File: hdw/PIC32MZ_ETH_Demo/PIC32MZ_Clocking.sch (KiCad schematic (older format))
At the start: 15 parts

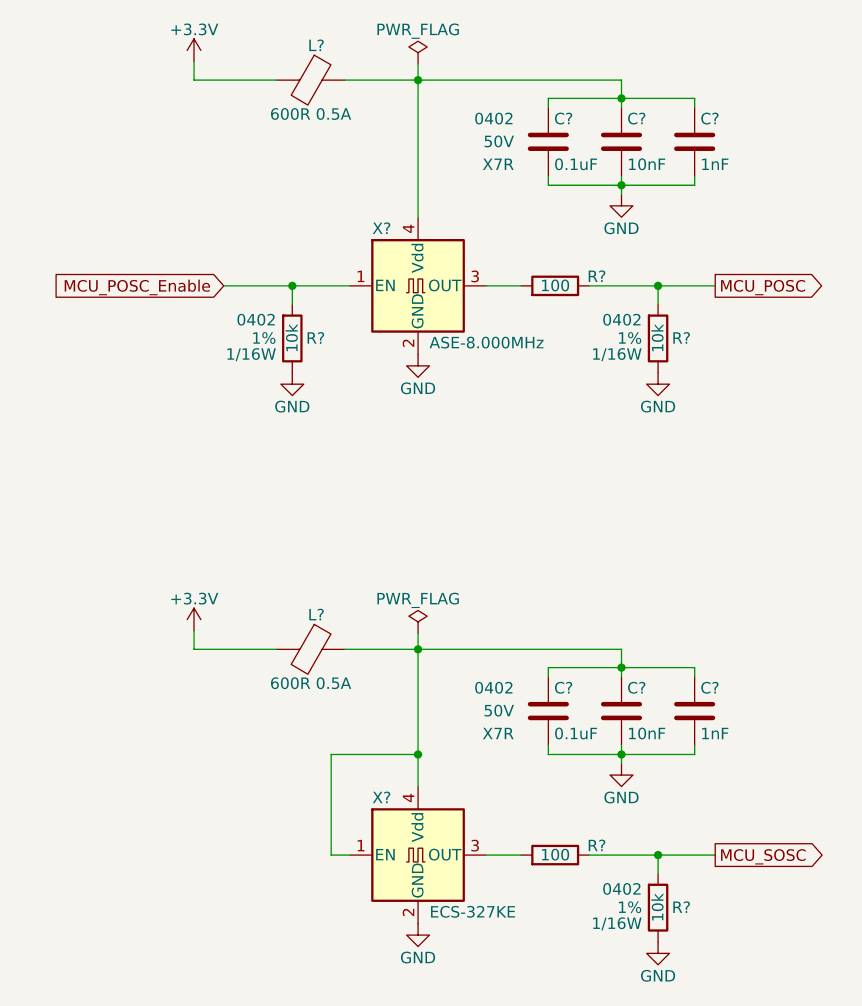
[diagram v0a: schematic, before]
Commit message: More schematic tweaks, followed PHY design guide
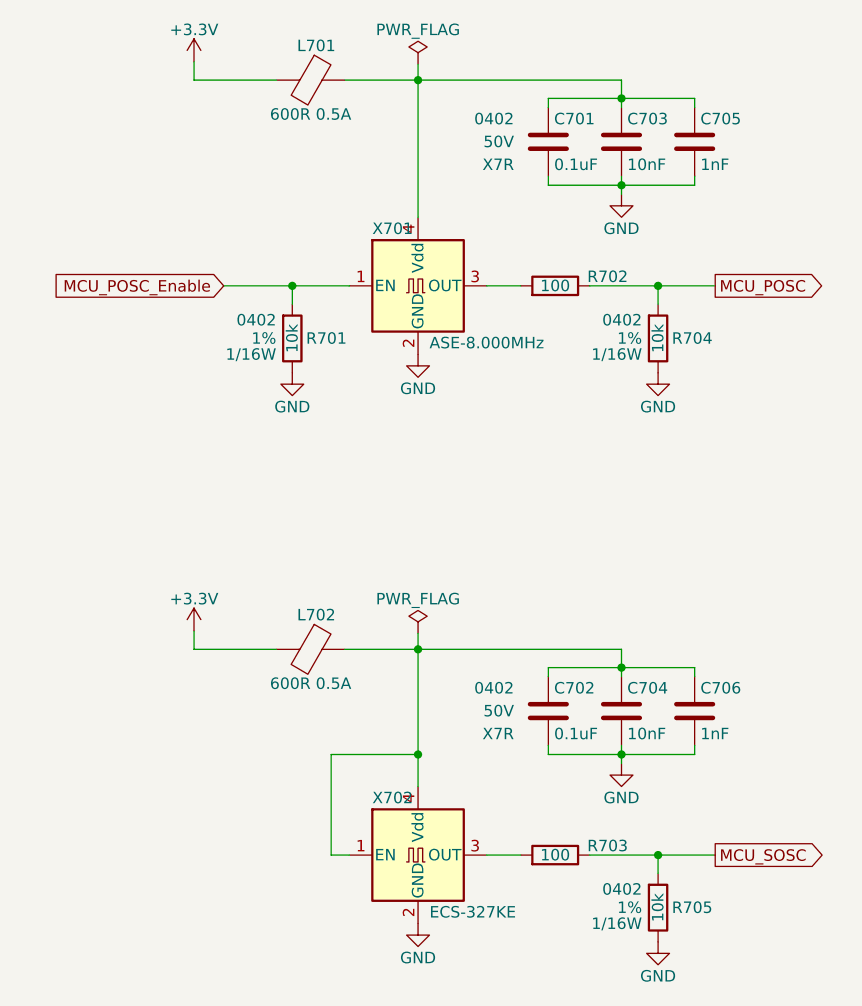
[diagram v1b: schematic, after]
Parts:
- gave numbers to parts that had none: 15
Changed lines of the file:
@@
 EESchema Schematic File Version 4
+LIBS:PIC32MZ_ETH_Demo-cache
 EELAYER 30 0
 EELAYER END
@@
 $EndDescr
 $Comp
-L Oscillator:ASE-xxxMHz X?
+L Oscillator:ASE-xxxMHz X701
 U 1 1 5E015C3C
 P 5510 2700
-F 0 "X?" H 5310 2950 50  0000 L CNN
+F 0 "X701" H 5310 2950 50  0000 L CNN
 F 1 "ASE-8.000MHz" H 5560 2450 50  0000 L CNN
 F 2 "Oscillator:Oscillator_SMD_Abracon_ASE-4Pin_3.2x2.5mm" H 6210 2350 50  0001 C CNN
@@
 $EndComp
 $Comp
-L power:GND #PWR?
+L power:GND #PWR0704
 U 1 1 5E01A3D9
 P 5510 3000
-F 0 "#PWR?" H 5510 2750 50  0001 C CNN
+F 0 "#PWR0704" H 5510 2750 50  0001 C CNN
 F 1 "GND" H 5510 2850 50  0000 C CNN
 F 2 "" H 5510 3000 50  0001 C CNN
@@
 AR Path="/5CB7A8BC/5E021EF5" Ref="R?"  Part="1"
 AR Path="/5E01BCC3/5E021EF5" Ref="R?"  Part="1"
-AR Path="/5E697952/5E021EF5" Ref="R?"  Part="1"
-F 0 "R?" H 6500 2930 50  0000 R CNN
+AR Path="/5E697952/5E021EF5" Ref="R704"  Part="1"
+F 0 "R704" H 6500 2930 50  0000 R CNN
 F 1 "10k" V 6560 2930 50  0000 C CNN
 F 2 "Resistors_SMD:R_0402" H 6560 2930 50  0001 C CNN
@@
 AR Path="/5CB7A8BC/5E021EFB" Ref="#PWR?"  Part="1"
 AR Path="/5E01BCC3/5E021EFB" Ref="#PWR?"  Part="1"
-AR Path="/5E697952/5E021EFB" Ref="#PWR?"  Part="1"
-F 0 "#PWR?" H 6560 2830 50  0001 C CNN
+AR Path="/5E697952/5E021EFB" Ref="#PWR0708"  Part="1"
+F 0 "#PWR0708" H 6560 2830 50  0001 C CNN
 F 1 "GND" H 6560 2930 50  0000 C CNN
 F 2 "" H 6560 3080 50  0001 C CNN
@@
 AR Path="/5CAD2DA3/5E024C29" Ref="R?"  Part="1"
 AR Path="/5E01BCC3/5E024C29" Ref="R?"  Part="1"
-AR Path="/5E697952/5E024C29" Ref="R?"  Part="1"
-F 0 "R?" V 6070 2560 50  0000 R CNN
+AR Path="/5E697952/5E024C29" Ref="R702"  Part="1"
+F 0 "R702" V 6070 2560 50  0000 R CNN
 F 1 "100" V 6110 2700 50  0000 C CNN
 F 2 "Resistors_SMD:R_0402" H 6110 2700 50  0001 C CNN
@@
 AR Path="/5CB7A8BC/5E0269C4" Ref="R?"  Part="1"
 AR Path="/5E01BCC3/5E0269C4" Ref="R?"  Part="1"
-AR Path="/5E697952/5E0269C4" Ref="R?"  Part="1"
-F 0 "R?" H 4900 2930 50  0000 R CNN
+AR Path="/5E697952/5E0269C4" Ref="R701"  Part="1"
+F 0 "R701" H 4900 2930 50  0000 R CNN
 F 1 "10k" V 4960 2930 50  0000 C CNN
 F 2 "Resistors_SMD:R_0402" H 4960 2930 50  0001 C CNN
@@
 AR Path="/5CB7A8BC/5E0269CA" Ref="#PWR?"  Part="1"
 AR Path="/5E01BCC3/5E0269CA" Ref="#PWR?"  Part="1"
-AR Path="/5E697952/5E0269CA" Ref="#PWR?"  Part="1"
-F 0 "#PWR?" H 4960 2830 50  0001 C CNN
+AR Path="/5E697952/5E0269CA" Ref="#PWR0703"  Part="1"
+F 0 "#PWR0703" H 4960 2830 50  0001 C CNN
 F 1 "GND" H 4960 2930 50  0000 C CNN
 F 2 "" H 4960 3080 50  0001 C CNN
@@
 AR Path="/5CB25152/5E03ADCE" Ref="#PWR?"  Part="1"
 AR Path="/5E01BCC3/5E03ADCE" Ref="#PWR?"  Part="1"
-AR Path="/5E697952/5E03ADCE" Ref="#PWR?"  Part="1"
-F 0 "#PWR?" H 6400 2050 50  0001 C CNN
+AR Path="/5E697952/5E03ADCE" Ref="#PWR0706"  Part="1"
+F 0 "#PWR0706" H 6400 2050 50  0001 C CNN
 F 1 "GND" H 6400 2150 50  0000 C CNN
 F 2 "" H 6400 2300 50  0000 C CNN
@@
 AR Path="/5CB25152/5E03ADD8" Ref="C?"  Part="1"
 AR Path="/5E01BCC3/5E03ADD8" Ref="C?"  Part="1"
-AR Path="/5E697952/5E03ADD8" Ref="C?"  Part="1"
-F 0 "C?" H 6105 2170 50  0000 L CNN
+AR Path="/5E697952/5E03ADD8" Ref="C701"  Part="1"
+F 0 "C701" H 6105 2170 50  0000 L CNN
 F 1 "0.1uF" H 6105 1970 50  0000 L CNN
 F 2 "Capacitors_SMD:C_0402" H 6118 1920 50  0001 C CNN
@@
 AR Path="/5CB25152/5E03ADE2" Ref="C?"  Part="1"
 AR Path="/5E01BCC3/5E03ADE2" Ref="C?"  Part="1"
-AR Path="/5E697952/5E03ADE2" Ref="C?"  Part="1"
-F 0 "C?" H 6745 2170 50  0000 L CNN
+AR Path="/5E697952/5E03ADE2" Ref="C705"  Part="1"
+F 0 "C705" H 6745 2170 50  0000 L CNN
 F 1 "1nF" H 6745 1970 50  0000 L CNN
 F 2 "Capacitors_SMD:C_0402" H 6758 1920 50  0001 C CNN
@@
 AR Path="/5CB25152/5E03ADEC" Ref="C?"  Part="1"
 AR Path="/5E01BCC3/5E03ADEC" Ref="C?"  Part="1"
-AR Path="/5E697952/5E03ADEC" Ref="C?"  Part="1"
-F 0 "C?" H 6425 2170 50  0000 L CNN
+AR Path="/5E697952/5E03ADEC" Ref="C703"  Part="1"
+F 0 "C703" H 6425 2170 50  0000 L CNN
 F 1 "10nF" H 6425 1970 50  0000 L CNN
 F 2 "Capacitors_SMD:C_0402" H 6438 1920 50  0001 C CNN
@@
 AR Path="/5CAD2D97/5E053473" Ref="L?"  Part="1"
 AR Path="/5E01BCC3/5E053473" Ref="L?"  Part="1"
-AR Path="/5E697952/5E053473" Ref="L?"  Part="1"
-F 0 "L?" V 4890 1825 50  0000 C CNN
+AR Path="/5E697952/5E053473" Ref="L701"  Part="1"
+F 0 "L701" V 4890 1825 50  0000 C CNN
 F 1 "600R 0.5A" V 5190 1800 50  0000 C CNN
 F 2 "Inductors_SMD:L_0603" V 4970 1800 50  0001 C CNN
@@
 	4530 1800 4890 1800
 $Comp
-L power:GND #PWR?
+L power:GND #PWR0705
 U 1 1 5E056297
 P 5510 5490
-F 0 "#PWR?" H 5510 5240 50  0001 C CNN
+F 0 "#PWR0705" H 5510 5240 50  0001 C CNN
 F 1 "GND" H 5510 5340 50  0000 C CNN
 F 2 "" H 5510 5490 50  0001 C CNN
@@
 AR Path="/5CB7A8BC/5E0562A6" Ref="R?"  Part="1"
 AR Path="/5E01BCC3/5E0562A6" Ref="R?"  Part="1"
-AR Path="/5E697952/5E0562A6" Ref="R?"  Part="1"
-F 0 "R?" H 6500 5420 50  0000 R CNN
+AR Path="/5E697952/5E0562A6" Ref="R705"  Part="1"
+F 0 "R705" H 6500 5420 50  0000 R CNN
 F 1 "10k" V 6560 5420 50  0000 C CNN
 F 2 "Resistors_SMD:R_0402" H 6560 5420 50  0001 C CNN
@@
 AR Path="/5CB7A8BC/5E0562B0" Ref="#PWR?"  Part="1"
 AR Path="/5E01BCC3/5E0562B0" Ref="#PWR?"  Part="1"
-AR Path="/5E697952/5E0562B0" Ref="#PWR?"  Part="1"
-F 0 "#PWR?" H 6560 5320 50  0001 C CNN
+AR Path="/5E697952/5E0562B0" Ref="#PWR0709"  Part="1"
+F 0 "#PWR0709" H 6560 5320 50  0001 C CNN
 F 1 "GND" H 6560 5420 50  0000 C CNN
 F 2 "" H 6560 5570 50  0001 C CNN
@@
 AR Path="/5CAD2DA3/5E0562C1" Ref="R?"  Part="1"
 AR Path="/5E01BCC3/5E0562C1" Ref="R?"  Part="1"
-AR Path="/5E697952/5E0562C1" Ref="R?"  Part="1"
-F 0 "R?" V 6070 5050 50  0000 R CNN
+AR Path="/5E697952/5E0562C1" Ref="R703"  Part="1"
+F 0 "R703" V 6070 5050 50  0000 R CNN
 F 1 "100" V 6110 5190 50  0000 C CNN
 F 2 "Resistors_SMD:R_0402" H 6110 5190 50  0001 C CNN
@@
 AR Path="/5CB25152/5E0562EA" Ref="#PWR?"  Part="1"
 AR Path="/5E01BCC3/5E0562EA" Ref="#PWR?"  Part="1"
-AR Path="/5E697952/5E0562EA" Ref="#PWR?"  Part="1"
-F 0 "#PWR?" H 6400 4540 50  0001 C CNN
+AR Path="/5E697952/5E0562EA" Ref="#PWR0707"  Part="1"
+F 0 "#PWR0707" H 6400 4540 50  0001 C CNN
 F 1 "GND" H 6400 4640 50  0000 C CNN
 F 2 "" H 6400 4790 50  0000 C CNN
@@
 AR Path="/5CB25152/5E0562F8" Ref="C?"  Part="1"
 AR Path="/5E01BCC3/5E0562F8" Ref="C?"  Part="1"
-AR Path="/5E697952/5E0562F8" Ref="C?"  Part="1"
-F 0 "C?" H 6105 4660 50  0000 L CNN
+AR Path="/5E697952/5E0562F8" Ref="C702"  Part="1"
+F 0 "C702" H 6105 4660 50  0000 L CNN
 F 1 "0.1uF" H 6105 4460 50  0000 L CNN
 F 2 "Capacitors_SMD:C_0402" H 6118 4410 50  0001 C CNN
@@
 AR Path="/5CB25152/5E056306" Ref="C?"  Part="1"
 AR Path="/5E01BCC3/5E056306" Ref="C?"  Part="1"
-AR Path="/5E697952/5E056306" Ref="C?"  Part="1"
-F 0 "C?" H 6745 4660 50  0000 L CNN
+AR Path="/5E697952/5E056306" Ref="C706"  Part="1"
+F 0 "C706" H 6745 4660 50  0000 L CNN
 F 1 "1nF" H 6745 4460 50  0000 L CNN
 F 2 "Capacitors_SMD:C_0402" H 6758 4410 50  0001 C CNN
@@
 AR Path="/5CB25152/5E056314" Ref="C?"  Part="1"
 AR Path="/5E01BCC3/5E056314" Ref="C?"  Part="1"
-AR Path="/5E697952/5E056314" Ref="C?"  Part="1"
-F 0 "C?" H 6425 4660 50  0000 L CNN
+AR Path="/5E697952/5E056314" Ref="C704"  Part="1"
+F 0 "C704" H 6425 4660 50  0000 L CNN
 F 1 "10nF" H 6425 4460 50  0000 L CNN
 F 2 "Capacitors_SMD:C_0402" H 6438 4410 50  0001 C CNN
@@
 AR Path="/5CAD2D97/5E05632C" Ref="L?"  Part="1"
 AR Path="/5E01BCC3/5E05632C" Ref="L?"  Part="1"
-AR Path="/5E697952/5E05632C" Ref="L?"  Part="1"
-F 0 "L?" V 4890 4315 50  0000 C CNN
+AR Path="/5E697952/5E05632C" Ref="L702"  Part="1"
+F 0 "L702" V 4890 4315 50  0000 C CNN
 F 1 "600R 0.5A" V 5190 4290 50  0000 C CNN
 F 2 "Inductors_SMD:L_0603" V 4970 4290 50  0001 C CNN
@@
 	4530 4290 4890 4290
 $Comp
-L Custom_Library:ECS-327KE X?
+L Custom_Library:ECS-327KE X702
 U 1 1 5E05D8E0
 P 5510 5190
-F 0 "X?" H 5310 5440 50  0000 L CNN
+F 0 "X702" H 5310 5440 50  0000 L CNN
 F 1 "ECS-327KE" H 5560 4940 50  0000 L CNN
 F 2 "Custom Footprints Library:ECS-327KE" H 6210 4840 50  0001 C CNN
@@
 	5510 4750 5510 4890
 $Comp
-L power:PWR_FLAG #FLG?
+L power:PWR_FLAG #FLG0702
 U 1 1 5E43B375
 P 5510 4220
-F 0 "#FLG?" H 5510 4295 50  0001 C CNN
+F 0 "#FLG0702" H 5510 4295 50  0001 C CNN
 F 1 "PWR_FLAG" H 5510 4370 50  0000 C CNN
 F 2 "" H 5510 4220 50  0001 C CNN
@@
 	5510 4220 5510 4290
 $Comp
-L power:PWR_FLAG #FLG?
+L power:PWR_FLAG #FLG0701
 U 1 1 5E43F288
 P 5510 1730
-F 0 "#FLG?" H 5510 1805 50  0001 C CNN
+F 0 "#FLG0701" H 5510 1805 50  0001 C CNN
 F 1 "PWR_FLAG" H 5510 1880 50  0000 C CNN
 F 2 "" H 5510 1730 50  0001 C CNN
@@
 	5510 1730 5510 1800
 $Comp
-L power:+3.3V #PWR?
+L power:+3.3V #PWR0701
 U 1 1 5E6E8CA9
 P 4530 1720
-F 0 "#PWR?" H 4530 1570 50  0001 C CNN
+F 0 "#PWR0701" H 4530 1570 50  0001 C CNN
 F 1 "+3.3V" H 4530 1860 50  0000 C CNN
 F 2 "" H 4530 1720 50  0001 C CNN
@@
 $EndComp
 $Comp
-L power:+3.3V #PWR?
+L power:+3.3V #PWR0702
 U 1 1 5E6E96AD
 P 4530 4210
-F 0 "#PWR?" H 4530 4060 50  0001 C CNN
+F 0 "#PWR0702" H 4530 4060 50  0001 C CNN
 F 1 "+3.3V" H 4530 4350 50  0000 C CNN
 F 2 "" H 4530 4210 50  0001 C CNN

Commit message: Populated digi-key pn's
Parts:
- C701, C702: Digi-Key PN (none) -> 490-10701-1-ND
- C703, C704: Digi-Key PN (none) -> 490-13295-1-ND
- C705, C706: Digi-Key PN (none) -> 399-1032-1-ND
- L701, L702: footprint Inductors_SMD:L_0603 -> Inductors_SMD:L_0402; Digi-Key PN (none) -> 490-5441-1-ND
- R701, R704, R705: Digi-Key PN (none) -> RMCF0402FT10K0CT-ND
- R702, R703: Digi-Key PN (none) -> 541-100LCT-ND
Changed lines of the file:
@@
 F 5 "1%" H 6630 2930 50  0000 L CNN "Tolerance"
 F 6 "1/16W" H 6630 2860 50  0000 L CNN "Wattage"
-F 7 "" H 6560 2930 50  0001 C CNN "Digi-Key PN"
+F 7 "RMCF0402FT10K0CT-ND" H 6560 2930 50  0001 C CNN "Digi-Key PN"
 	1    6560 2930
 	-1   0    0    -1
@@
 F 5 "1%" V 6310 2700 50  0001 C CNN "Tolerance"
 F 6 "1/16W" V 6410 2700 50  0001 C CNN "Wattage"
-F 7 "" H 6410 3100 60  0001 C CNN "Digi-Key PN"
+F 7 "541-100LCT-ND" H 6410 3100 60  0001 C CNN "Digi-Key PN"
 	1    6110 2700
 	0    -1   1    0
@@
 F 5 "1%" H 5030 2930 50  0000 L CNN "Tolerance"
 F 6 "1/16W" H 5030 2860 50  0000 L CNN "Wattage"
-F 7 "" H 4960 2930 50  0001 C CNN "Digi-Key PN"
+F 7 "RMCF0402FT10K0CT-ND" H 4960 2930 50  0001 C CNN "Digi-Key PN"
 	1    4960 2930
 	-1   0    0    -1
@@
 F 5 "50V" H 5930 2070 50  0000 R CNN "Voltage"
 F 6 "X7R" H 5930 1970 50  0000 R CNN "Dielectric"
-F 7 "" H 2170 -4810 50  0001 C CNN "Digi-Key PN"
+F 7 "490-10701-1-ND" H 2170 -4810 50  0001 C CNN "Digi-Key PN"
 	1    6080 2070
 	1    0    0    -1
@@
 F 5 "50V" H 6570 2070 50  0001 R CNN "Voltage"
 F 6 "X7R" H 6570 1970 50  0001 R CNN "Dielectric"
-F 7 "" H 2170 -4810 50  0001 C CNN "Digi-Key PN"
+F 7 "399-1032-1-ND" H 2170 -4810 50  0001 C CNN "Digi-Key PN"
 	1    6720 2070
 	1    0    0    -1
@@
 F 5 "50V" H 6250 2070 50  0001 R CNN "Voltage"
 F 6 "X7R" H 6250 1970 50  0001 R CNN "Dielectric"
-F 7 "" H 2170 -4810 50  0001 C CNN "Digi-Key PN"
+F 7 "490-13295-1-ND" H 2170 -4810 50  0001 C CNN "Digi-Key PN"
 	1    6400 2070
 	1    0    0    -1
@@
 F 0 "L701" V 4890 1825 50  0000 C CNN
 F 1 "600R 0.5A" V 5190 1800 50  0000 C CNN
-F 2 "Inductors_SMD:L_0603" V 4970 1800 50  0001 C CNN
+F 2 "Inductors_SMD:L_0402" V 4970 1800 50  0001 C CNN
 F 3 "~" H 5040 1800 50  0001 C CNN
-F 4 "" H -3150 -1290 50  0001 C CNN "Digi-Key PN"
+F 4 "490-5441-1-ND" H -3150 -1290 50  0001 C CNN "Digi-Key PN"
 	1    5040 1800
 	0    1    1    0
@@
 F 5 "1%" H 6630 5420 50  0000 L CNN "Tolerance"
 F 6 "1/16W" H 6630 5350 50  0000 L CNN "Wattage"
-F 7 "" H 6560 5420 50  0001 C CNN "Digi-Key PN"
+F 7 "RMCF0402FT10K0CT-ND" H 6560 5420 50  0001 C CNN "Digi-Key PN"
 	1    6560 5420
 	-1   0    0    -1
@@
 F 5 "1%" V 6310 5190 50  0001 C CNN "Tolerance"
 F 6 "1/16W" V 6410 5190 50  0001 C CNN "Wattage"
-F 7 "" H 6410 5590 60  0001 C CNN "Digi-Key PN"
+F 7 "541-100LCT-ND" H 6410 5590 60  0001 C CNN "Digi-Key PN"
 	1    6110 5190
 	0    -1   1    0
@@
 F 5 "50V" H 5930 4560 50  0000 R CNN "Voltage"
 F 6 "X7R" H 5930 4460 50  0000 R CNN "Dielectric"
-F 7 "" H 2170 -2320 50  0001 C CNN "Digi-Key PN"
+F 7 "490-10701-1-ND" H 2170 -2320 50  0001 C CNN "Digi-Key PN"
 	1    6080 4560
 	1    0    0    -1
@@
 F 5 "50V" H 6570 4560 50  0001 R CNN "Voltage"
 F 6 "X7R" H 6570 4460 50  0001 R CNN "Dielectric"
-F 7 "" H 2170 -2320 50  0001 C CNN "Digi-Key PN"
+F 7 "399-1032-1-ND" H 2170 -2320 50  0001 C CNN "Digi-Key PN"
 	1    6720 4560
 	1    0    0    -1
@@
 F 5 "50V" H 6250 4560 50  0001 R CNN "Voltage"
 F 6 "X7R" H 6250 4460 50  0001 R CNN "Dielectric"
-F 7 "" H 2170 -2320 50  0001 C CNN "Digi-Key PN"
+F 7 "490-13295-1-ND" H 2170 -2320 50  0001 C CNN "Digi-Key PN"
 	1    6400 4560
 	1    0    0    -1
@@
 F 0 "L702" V 4890 4315 50  0000 C CNN
 F 1 "600R 0.5A" V 5190 4290 50  0000 C CNN
-F 2 "Inductors_SMD:L_0603" V 4970 4290 50  0001 C CNN
+F 2 "Inductors_SMD:L_0402" V 4970 4290 50  0001 C CNN
 F 3 "~" H 5040 4290 50  0001 C CNN
-F 4 "" H -3150 1200 50  0001 C CNN "Digi-Key PN"
+F 4 "490-5441-1-ND" H -3150 1200 50  0001 C CNN "Digi-Key PN"
 	1    5040 4290
 	0    1    1    0
